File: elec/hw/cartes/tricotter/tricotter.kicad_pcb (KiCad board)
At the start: 2 copper layers, 55 x 155 mm, 77 parts, among them J1 XT60PW-M, J10 3-794618-4, J11 3-794618-4, J12 3-794618-4, J2 XT60PW-M, J3 XT60PW-M, J5 22053041, J8 3-794618-4, J9 3-794618-4, Q11 G120P06M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

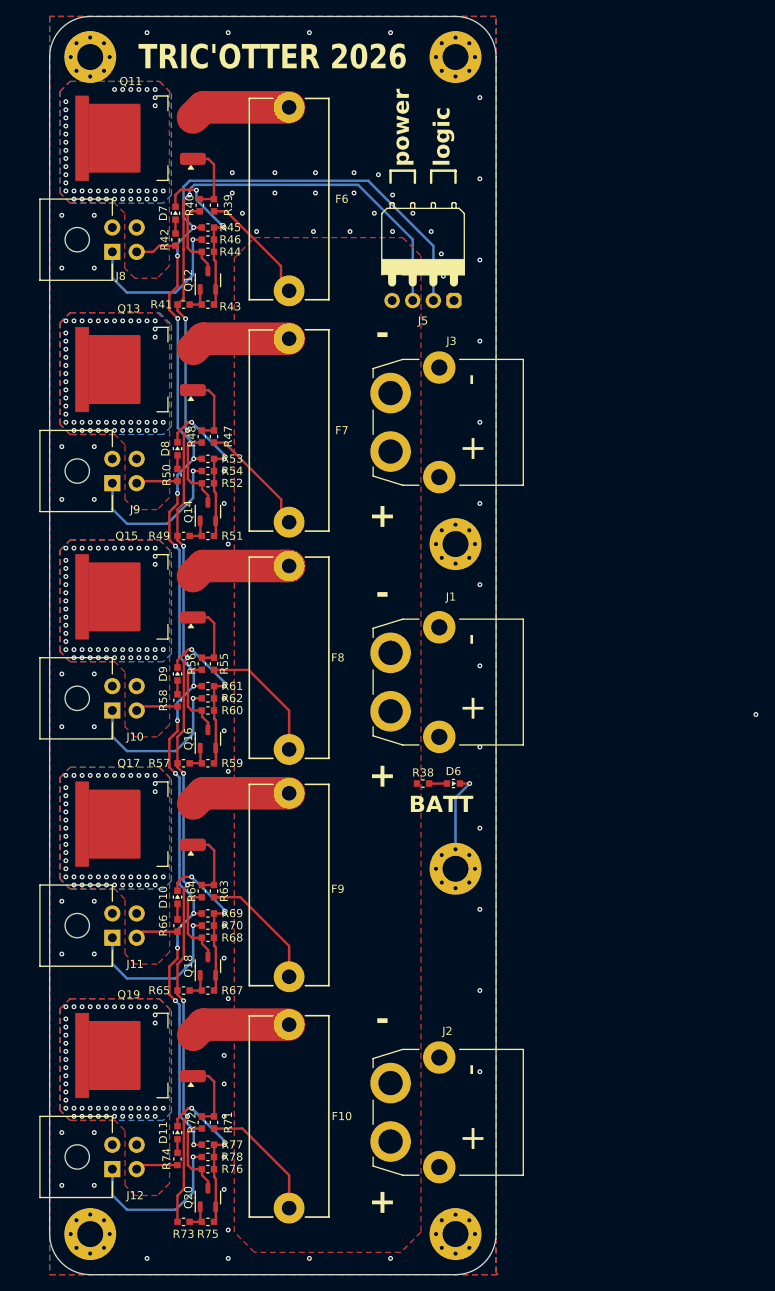
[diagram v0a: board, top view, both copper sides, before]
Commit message: tricotter : reduced from 5 to 3 power channel and added chaining connector
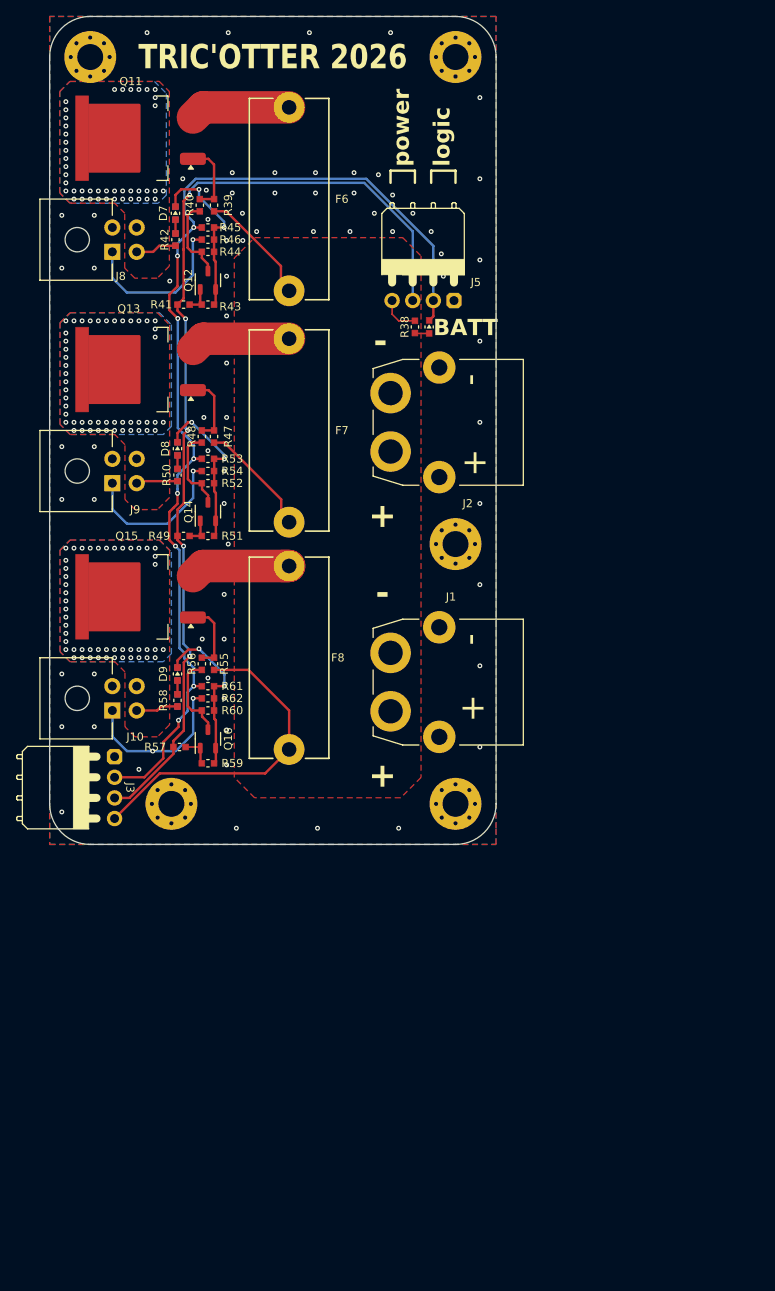
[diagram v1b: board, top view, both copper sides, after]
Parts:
- removed D10, D11: green, 0603, cocotter_diodes:LED_0603_1608Metric
- removed F10, F9: FH1-200CK-B, cocotter_others:FUSEHOLDER_5x20mm
- removed H6: MountingHole_Pad_M3, cocotter_others:MountingHole_3.2mm_M3_Pad_Via
- removed J11, J12: 3-794618-4, cocotter_connectors:3-794618-4
- removed Q17, Q19: G120P06M, cocotter_transistors:TO-263-2-GOFORD
- removed Q18, Q20: 2N7002, cocotter_transistors:SOT-23-3
- removed R63, R64, R65, R67, R71, R72, R73, R75: 100k, cocotter_resistor:r0603_reflow
- removed R66, R74: 10k 1%, cocotter_resistor:r0603_reflow
- removed R68, R69, R70, R76, R77, R78: 0R, cocotter_resistor:r0603_reflow
- added D1: green, 0603, cocotter_diodes:LED_0603_1608Metric, B.Cu at (115.5, 49.2)
- added D2: green, 0603, cocotter_diodes:LED_0603_1608Metric, B.Cu at (115.8, 78.2)
- added D3: green, 0603, cocotter_diodes:LED_0603_1608Metric, B.Cu at (115.8, 106.0)
- added R1: 10k 1%, cocotter_resistor:r0603_reflow, B.Cu at (115.5, 52.5)
- added R2: 10k 1%, cocotter_resistor:r0603_reflow, B.Cu at (115.8, 81.5)
- added R3: 10k 1%, cocotter_resistor:r0603_reflow, B.Cu at (115.8, 109.2)
- J3: value XT60PW-M -> 22053041; footprint cocotter_connectors:XT60PW-M -> cocotter_connectors:22053041
- moved J2 85.0 mm to (142.0, 75.0)
- moved J3 56.4 mm to (108.0, 120.0)
- moved D6 56.3 mm to (146.8, 63.2), turned to -90 degrees
- moved R38 56.3 mm to (145.0, 63.2), turned to -90 degrees
- moved H1 53.9 mm to (115.0, 122.0)
- moved H2 53.0 mm to (150.0, 122.0)
- moved R57 2.06 mm to (116.0, 115.0)
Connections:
- D6 pad C: GND -> /SW_logical
- J3 pad 4: (no net) -> +BATT
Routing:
- net GND: track 113.0 -> 60.1 mm, vias 82 -> 76
- net /SW_POWER: track 170.0 -> 120.9 mm, vias 9 -> 5
- net /SW_logical: track 174.6 -> 131.5 mm, vias 13 -> 8
- net Net-(Q20-S): track 20.5 -> 0.00 mm, vias 2 -> 0
- net Net-(Q18-S): track 20.1 -> 0.00 mm, vias 2 -> 0
- net Net-(Q19-S): track 12.4 -> 0.00 mm
- net Net-(Q17-S): track 12.4 -> 0.00 mm
- net Net-(Q20-D): track 10.6 -> 0.00 mm
- net Net-(Q18-D): track 10.6 -> 0.00 mm
- net Net-(Q19-G): track 8.89 -> 0.00 mm
- net Net-(Q17-G): track 8.89 -> 0.00 mm
- net Net-(Q17-D): track 7.34 -> 0.00 mm, vias 49 -> 0
- net Net-(Q19-D): track 6.23 -> 0.00 mm, vias 49 -> 0
- net Net-(Q20-G): track 3.45 -> 0.00 mm
- net Net-(Q18-G): track 3.45 -> 0.00 mm
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- removed copper zone on B.Cu, net Net-(Q17-D)
- removed copper zone on F.Cu, net Net-(Q17-D)
- removed copper zone on B.Cu, net Net-(Q19-D)
- removed copper zone on F.Cu, net Net-(Q19-D)
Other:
- board size 55 x 155 mm -> 55 x 102 mm
